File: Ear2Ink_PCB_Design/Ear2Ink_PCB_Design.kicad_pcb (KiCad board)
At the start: 2 copper layers, 108 x 82.5 mm, 84 parts, among them J1 Conn_01x16_Pin, J2 Conn_01x08_Pin, J3 Conn_01x08_Pin, J4 MEM2052-00-195-00-A_REVA, J5 Conn_01x06_Pin, J6 Conn_01x04_Pin, J8 Conn_01x16_Pin, P1 OSTTE020104, SW1 SW_Push, U1 STM32F411RETx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

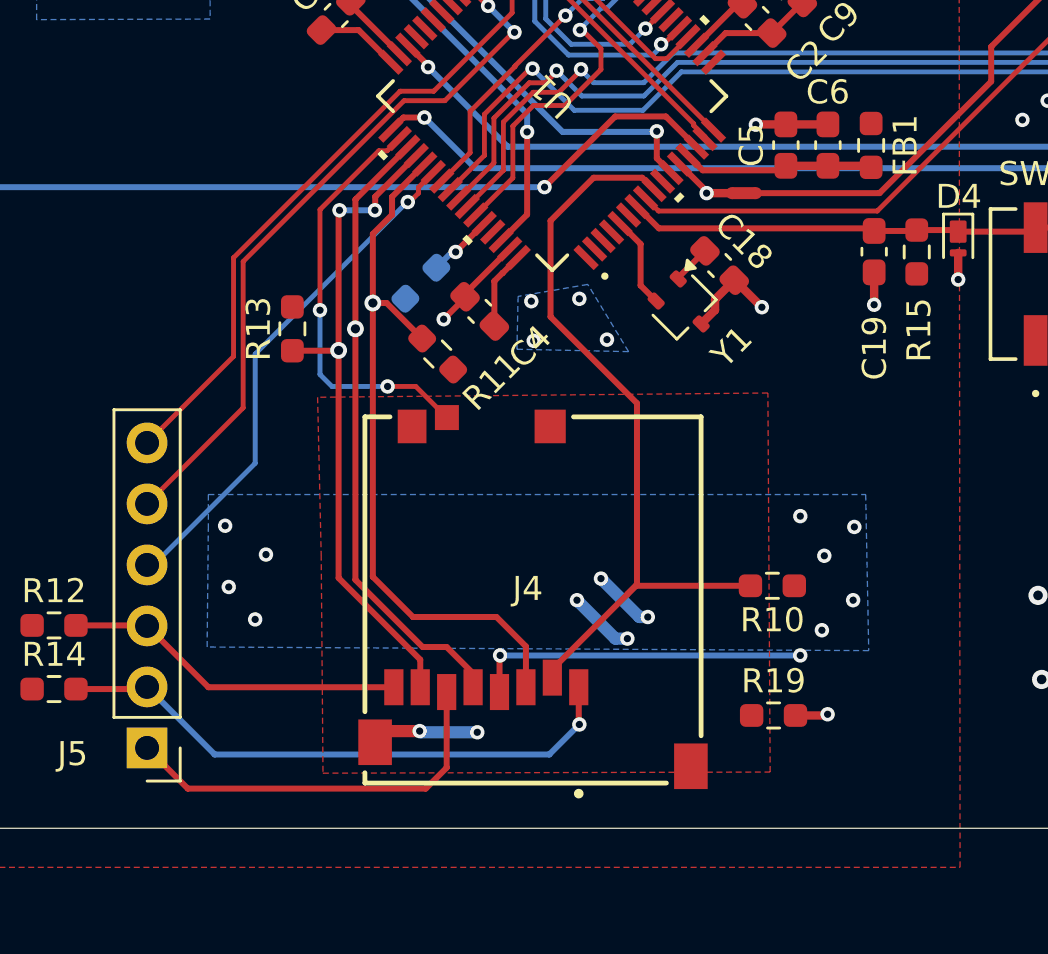
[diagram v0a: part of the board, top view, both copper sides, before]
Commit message: flipped SD to the other side
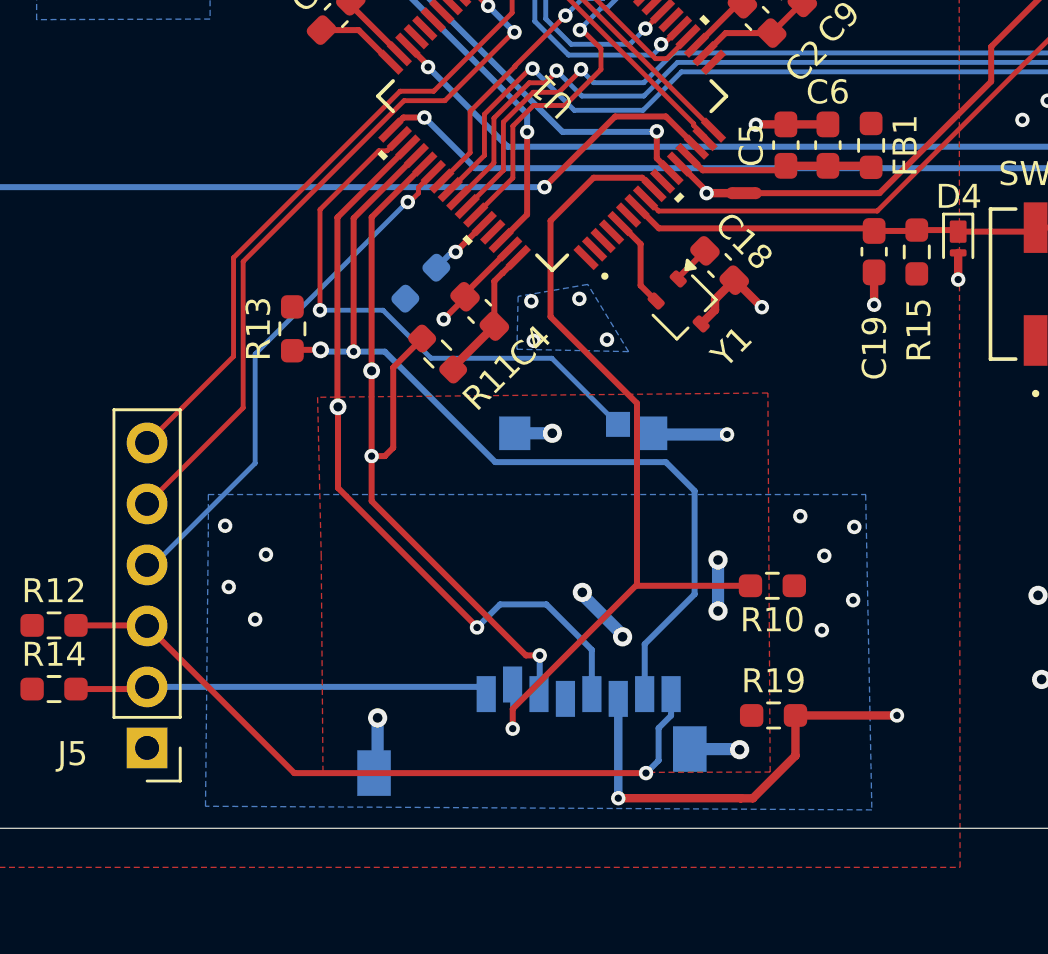
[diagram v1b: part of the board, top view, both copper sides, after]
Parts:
- J4: moved to B.Cu
- moved J4 0.29 mm to (144.7, 92.4), turned to 180 degrees
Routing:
- net SD_DAT1: track 14.3 -> 30.0 mm, vias 0 -> 1
- net +3.3V: track 50.6 -> 39.1 mm, vias 35 -> 33
- net SPI3_MISO: track 27.8 -> 37.7 mm, vias 3 -> 2
- net SD_DAT2: track 24.2 -> 17.2 mm, vias 1 -> 0
- net SD_Detect: track 17.5 -> 23.2 mm, vias 2 -> 1
- net SPI3_SCK: track 26.0 -> 31.4 mm, vias 1 -> 2
- net CS: track 32.2 -> 36.6 mm, vias 0 -> 1
- net Net-(J4-SHIELD_GND): track 9.84 -> 13.8 mm, vias 6 -> 8
- net SPI3_MOSI: track 30.0 -> 32.3 mm, vias 1 -> 3
- net GND: track 75.7 -> 75.8 mm, vias 183 -> 184

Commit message: added pic
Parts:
- added G***: LOGO, LOGO, F.Cu at (106.8, 86.3)

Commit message: fab outputs
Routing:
- net +3.3V: vias 33 -> 38
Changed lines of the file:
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@@
 			(outputformat 1)
 			(mirror no)
-			(drillshape 1)
+			(drillshape 0)
 			(scaleselection 1)
-			(outputdirectory "")
+			(outputdirectory "Fab_Outputs/")
 		)
 	)
@@
 			(keep_text_aligned yes)
 		)
-		(gr_text "3.25"
+		(gr_text "3250"
 			(at 196.05 60.325 90)
 			(layer "F.CrtYd")
@@
 			(keep_text_aligned yes)
 		)
-		(gr_text "0.6693"
+		(gr_text "669.2913"
 			(at 189.95 36.15 90)
 			(layer "F.CrtYd")
@@
 			(keep_text_aligned yes)
 		)
-		(gr_text "4.25"
+		(gr_text "4250"
 			(at 136.525 113.3 0)
 			(layer "F.CrtYd")
@@
 			(keep_text_aligned yes)
 		)
-		(gr_text "2.5606"
+		(gr_text "2560.6299"
 			(at 189.95 60.17 90)
 			(layer "F.CrtYd")
@@
 			(keep_text_aligned yes)
 		)
-		(gr_text "2.4823"
+		(gr_text "2482.2835"
 			(at 159.575 26.5 0)
 			(layer "F.CrtYd")
@@
 			(keep_text_aligned yes)
 		)
-		(gr_text "0.3209"
+		(gr_text "320.8661"
 			(at 189.9 23.575 90)
 			(layer "F.CrtYd")
@@
 	)
 	(via
+		(at 156.35 99.8)
+		(size 0.6)
+		(drill 0.3)
+		(layers "F.Cu" "B.Cu")
+		(free yes)
+		(net 2)
+	)
+	(via
+		(at 134.475 94.425)
+		(size 0.6)
+		(drill 0.3)
+		(layers "F.Cu" "B.Cu")
+		(free yes)
+		(net 2)
+	)
+	(via
 		(at 144.65 79.65)
 		(size 0.6)
@@
 	)
 	(via
+		(at 157.55 98.3)
+		(size 0.6)
+		(drill 0.3)
+		(layers "F.Cu" "B.Cu")
+		(free yes)
+		(net 2)
+	)
+	(via
 		(at 141.25 60.7)
 		(size 0.6)
@@
 	)
 	(via
+		(at 134.425 97)
+		(size 0.6)
+		(drill 0.3)
+		(layers "F.Cu" "B.Cu")
+		(free yes)
+		(net 2)
+	)
+	(via
 		(at 158.2 61)
 		(size 0.6)
 		(drill 0.3)
+		(layers "F.Cu" "B.Cu")
+		(free yes)
+		(net 2)
+	)
+	(via
+		(at 132.225 99.325)
+		(size 0.6)
+		(drill 0.3)
